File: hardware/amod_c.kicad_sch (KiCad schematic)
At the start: 209 parts, among them J1001 SMA, J1002 SMA, J1003 CE, J101 USB-C, J102 rails, J1101 SMA, J1102 SMA, J1201 SMA, J1202 SMA, J201 SMA, J202 SMA, J203 SMA, J204 SMA, J301 SMA, J302 SMA, J401 SMA, J402 SMA, J501 SMA, J502 SMA, J601 SMA, J602 SMA, J603 SMA, J701 SMA, J702 SMA, J801 SMA, J802 SMA, J901 SMA, J902 SMA, J903 SMA, J904 Pmod, Q1001 AO3401A, Q1002 DMMT3904W, Q1003 MMBT3904, Q1101 AO3401A, Q1201 AO3401A, Q201 AO3401A, Q202 AO3400A, Q301 AO3401A, Q401 AO3401A, Q501 AO3401A, Q601 AO3401A, Q701 AO3401A, Q801 AO3401A, Q901 AO3401A, Q902 BCM857BS, Q903 DMMT3904W, Q904 MMBT3904, SW1001 ON, SW1101 ON, SW1201 ON, SW201 ON, SW301 ON, SW401 ON, SW501 ON, SW601 ON, SW701 ON, SW801 ON, SW901 ON, U101 LM2664, U102 3.3V, U1101 TLC555, U1201 OPA2197, U201 TLV62568, U202 TPS7A2033, U203 OPA810, U301 LV1T34, U302 ICL7660A, U401 MAX7410, U402 LV1T34, U501 TMUX4053, U502 OPA810, U601 OPA2810, U602 TLV3501, U603 74LVC1G79, U604 74LVC1G3157, U605 74LVC1G3157, U701 LF398, U801 TLV3201, U901 OPA810

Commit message: AMOD-C: DRC 0 (Prompt 19). The Pmod's eight lines in lanes that never cross (the IOs reassigned so they nest: c5 IO8/IO4, c4 IO3, c8 IO2 down the left margin; c6 IO1/IO7, c7 IO5, c3 IO6 along the bottom); c6's bit and clock routed to its corner; the scope ground loops in the right margin
Co-Authored-By: Claude Opus 5.5 <noreply@anthropic.com>
Claude-Session: https://claude.ai/code/session_01RKeoKvFFzjk3cEBLCXXHnB
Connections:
- net PMOD1: now also U603.2 (C); no longer U701.11 (Hold)
- net PMOD5: now also U701.11 (Hold); no longer U603.2 (C)
- net PMOD6: now also U301.2 (A); no longer U603.4 (Q), U604.6 (S), U605.6 (S)
- net PMOD7: now also U603.4 (Q), U604.6 (S), U605.6 (S); no longer U301.2 (A)
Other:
- note added: "Clock IO1 at about 1 MHz and count IO7's ones. The second integrator pushes the quantization noise up at 40 dB per"
- note added: "EXPECT: OUT follows IN while IO5 is high and holds when it falls: 4 us to acquire, about 30 mV/s of droop, a few mV of hold step"
- note added: "EXPECT: a one-bit stream on IO7 whose density follows IN (+-1.65 V full scale), its noise shaped at 40 dB per decade"
- note added: "EXPECT: about -5 V on the output, falling with load as 1 / (f C) + the switches: 2 k at 1 kHz, 80 ohm at 100 kHz (the pump at half IO6's clock)"
- note added: "ICL7660A: switches charge the flying 1 uF across the supply and dump it, upside down, into the output's 1 uF. IO6"
- note added: "holding, and the aperture delay against the FPGA's edge on IO5."
- note removed: "Clock IO5 at about 1 MHz and count IO6's ones. The second integrator pushes the quantization noise up at 40 dB per"
- note removed: "EXPECT: OUT follows IN while IO1 is high and holds when it falls: 4 us to acquire, about 30 mV/s of droop, a few mV of hold step"
- note removed: "EXPECT: a one-bit stream on IO6 whose density follows IN (+-1.5 V full scale), its noise shaped at 40 dB per decade"
- note removed: "EXPECT: about -5 V on the output, falling with load as 1 / (f C) + the switches: 2 k at 1 kHz, 80 ohm at 100 kHz (the pump at half IO7's clock)"
- note removed: "ICL7660A: switches charge the flying 1 uF across the supply and dump it, upside down, into the output's 1 uF. IO7"
- note removed: "holding, and the aperture delay against the FPGA's edge on IO1."
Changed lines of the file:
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@@
 		)
 	)
-	(text "ICL7660A: switches charge the flying 1 uF across the supply and dump it, upside down, into the output's 1 uF.  IO7"
+	(text "ICL7660A: switches charge the flying 1 uF across the supply and dump it, upside down, into the output's 1 uF.  IO6"
 		(exclude_from_sim no)
 		(at 599.44 401.22 0)
@@
 		)
 	)
-	(text "holding, and the aperture delay against the FPGA's edge on IO1."
+	(text "holding, and the aperture delay against the FPGA's edge on IO5."
 		(exclude_from_sim no)
 		(at 599.44 530.86 0)
@@
 		)
 	)
-	(text "EXPECT: a one-bit stream on IO6 whose density follows IN (+-1.5 V full scale), its noise shaped at 40 dB per decade"
+	(text "EXPECT: a one-bit stream on IO7 whose density follows IN (+-1.65 V full scale), its noise shaped at 40 dB per decade"
 		(exclude_from_sim no)
 		(at 218.44 271.58 0)
@@
 		)
 	)
-	(text "EXPECT: about -5 V on the output, falling with load as 1 / (f C) + the switches: 2 k at 1 kHz, 80 ohm at 100 kHz (the pump at half IO7's clock)"
+	(text "Clock IO1 at about 1 MHz and count IO7's ones.  The second integrator pushes the quantization noise up at 40 dB per"
+		(exclude_from_sim no)
+		(at 218.44 274.22 0)
+		(effects
+			(font
+				(size 1.2 1.2)
+			)
+			(justify left)
+		)
+	)
+	(text "EXPECT: about -5 V on the output, falling with load as 1 / (f C) + the switches: 2 k at 1 kHz, 80 ohm at 100 kHz (the pump at half IO6's clock)"
 		(exclude_from_sim no)
 		(at 599.44 398.58 0)
@@
 		)
 	)
-	(text "Clock IO5 at about 1 MHz and count IO6's ones.  The second integrator pushes the quantization noise up at 40 dB per"
-		(exclude_from_sim no)
-		(at 218.44 274.22 0)
-		(effects
-			(font
-				(size 1.2 1.2)
-			)
-			(justify left)
-		)
-	)
 	(text "tutorial Trading speed for bits   (+-5 V)"
 		(exclude_from_sim no)
@@
 		)
 	)
-	(text "EXPECT: OUT follows IN while IO1 is high and holds when it falls: 4 us to acquire, about 30 mV/s of droop, a few mV of hold step"
+	(text "EXPECT: OUT follows IN while IO5 is high and holds when it falls: 4 us to acquire, about 30 mV/s of droop, a few mV of hold step"
 		(exclude_from_sim no)
 		(at 599.44 522.94 0)
@@
 		)
 	)
-	(label "PMOD6"
-		(at 449.58 198.12 0)
-		(effects
-			(font
-				(size 1.27 1.27)
-			)
-			(justify left)
-		)
-	)
 	(label "c5_VS"
 		(at 289.56 101.6 180)
@@
 		)
 	)
-	(label "PMOD6"
-		(at 500.38 200.66 180)
-		(effects
-			(font
-				(size 1.27 1.27)
-			)
-			(justify right)
-		)
-	)
 	(label "c9_MO"
 		(at 129.54 461.01 0)
@@
 		)
 	)
+	(label "PMOD7"
+		(at 449.58 198.12 0)
+		(effects
+			(font
+				(size 1.27 1.27)
+			)
+			(justify left)
+		)
+	)
 	(label "c5_OA"
 		(at 363.22 101.6 0)
@@
 		)
 	)
+	(label "PMOD1"
+		(at 419.1 208.28 180)
+		(effects
+			(font
+				(size 1.27 1.27)
+			)
+			(justify right)
+		)
+	)
 	(label "c7_VS"
 		(at 688.34 447.04 0)
@@
 		)
 	)
+	(label "PMOD7"
+		(at 464.82 200.66 180)
+		(effects
+			(font
+				(size 1.27 1.27)
+			)
+			(justify right)
+		)
+	)
 	(label "c5_VS"
 		(at 360.68 73.66 0)
@@
 		)
 	)
-	(label "PMOD1"
-		(at 680.72 457.2 180)
-		(effects
-			(font
-				(size 1.27 1.27)
-			)
-			(justify right)
-		)
-	)
 	(label "c1_CC1"
 		(at 660.4 180.34 0)
@@
 		)
 	)
+	(label "PMOD5"
+		(at 680.72 457.2 180)
+		(effects
+			(font
+				(size 1.27 1.27)
+			)
+			(justify right)
+		)
+	)
 	(label "c2_VS"
 		(at 287.02 322.58 0)
@@
 		)
 	)
-	(label "PMOD5"
-		(at 419.1 208.28 180)
-		(effects
-			(font
-				(size 1.27 1.27)
-			)
-			(justify right)
-		)
-	)
 	(label "c1_LEDR"
 		(at 642.62 254 180)
@@
 		)
 	)
-	(label "PMOD6"
-		(at 464.82 200.66 180)
-		(effects
-			(font
-				(size 1.27 1.27)
-			)
-			(justify right)
-		)
-	)
 	(label "c5_G"
 		(at 248.92 76.2 180)
@@
 		)
 	)
+	(label "PMOD6"
+		(at 680.72 330.2 180)
+		(effects
+			(font
+				(size 1.27 1.27)
+			)
+			(justify right)
+		)
+	)
 	(label "c8_VS"
 		(at 129.54 327.66 0)
@@
 		)
 	)
-	(label "PMOD7"
-		(at 680.72 330.2 180)
+	(label "c2_GATE"
+		(at 373.38 365.76 0)
 		(effects
 			(font
 				(size 1.27 1.27)
 			)
-			(justify right)
+			(justify left)
 		)
 	)
-	(label "c2_GATE"
-		(at 373.38 365.76 0)
+	(label "PMOD7"
+		(at 500.38 200.66 180)
 		(effects
 			(font
 				(size 1.27 1.27)
 			)
-			(justify left)
+			(justify right)
 		)
 	)

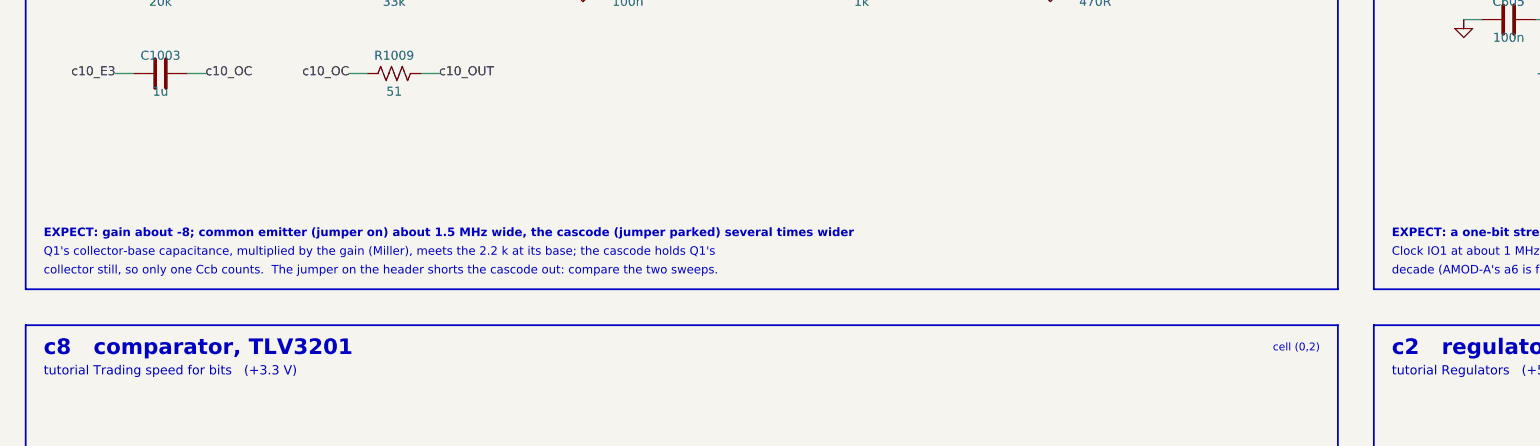
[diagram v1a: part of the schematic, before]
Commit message: AMOD-C: handbook, tile docs, Pmod line names and the README's table; JLCPCB rotations for its fifteen new codes (check_rotations: 209 codes, 0 differ); c10's gain stated from IN (-6) as well as at the collector; fab package
Co-Authored-By: Claude Opus 5.5 <noreply@anthropic.com>
Claude-Session: https://claude.ai/code/session_01RKeoKvFFzjk3cEBLCXXHnB
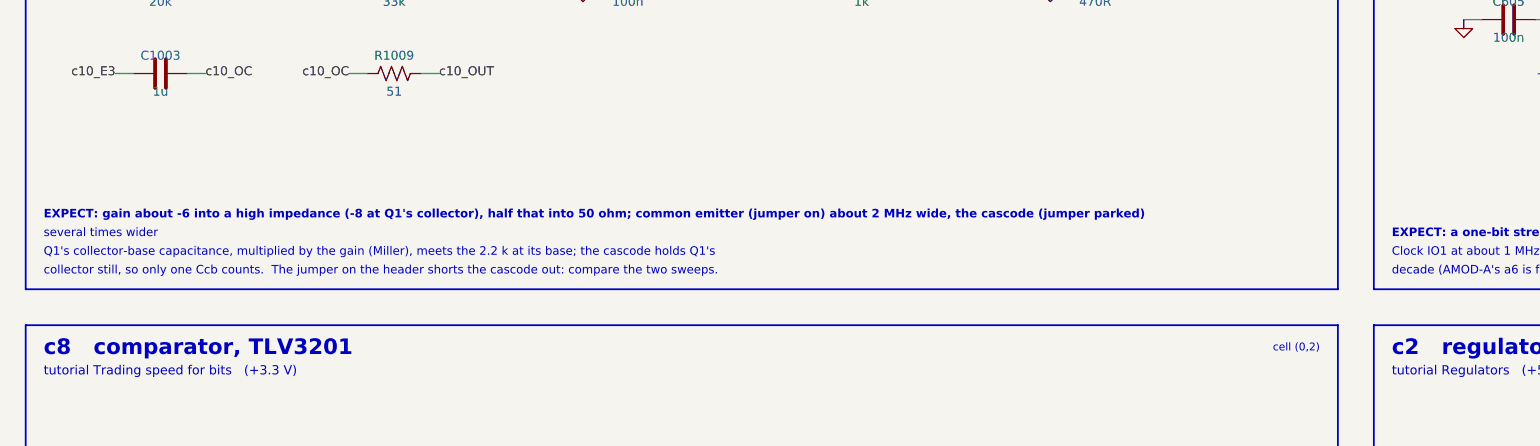
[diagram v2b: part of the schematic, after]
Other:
- note added: "EXPECT: gain about -6 into a high impedance (-8 at Q1's collector), half that into 50 ohm; common emitter (jumper on) about 2 MHz wide, the cascode (jumper parked)"
- note added: "several times wider"
- note removed: "EXPECT: gain about -8; common emitter (jumper on) about 1.5 MHz wide, the cascode (jumper parked) several times wider"
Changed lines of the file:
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@@
+		)
+	)
+	(text "Q1's collector-base capacitance, multiplied by the gain (Miller), meets the 2.2 k at its base; the cascode holds Q1's"
+		(exclude_from_sim no)
+		(at 27.94 274.22 0)
+		(effects
+			(font
+				(size 1.2 1.2)
+			)
+			(justify left)
 		)
 	)
@@
 		)
 	)
+	(text "several times wider"
+		(exclude_from_sim no)
+		(at 27.94 271.58 0)
+		(effects
+			(font
+				(size 1.2 1.2)
+			)
+			(justify left)
+		)
+	)
 	(text "±1 V"
 		(exclude_from_sim no)
@@
 		)
 	)
-	(text "Q1's collector-base capacitance, multiplied by the gain (Miller), meets the 2.2 k at its base; the cascode holds Q1's"
-		(exclude_from_sim no)
-		(at 27.94 274.22 0)
-		(effects
-			(font
-				(size 1.2 1.2)
-			)
-			(justify left)
-		)
-	)
 	(text "INT1"
 		(exclude_from_sim no)
@@
 		)
 	)
-	(text "EXPECT: gain about -8; common emitter (jumper on) about 1.5 MHz wide, the cascode (jumper parked) several times wider"
-		(exclude_from_sim no)
-		(at 27.94 271.58 0)
-		(effects
-			(font
-				(size 1.2 1.2)
-				(bold yes)
-			)
-			(justify left)
-		)
-	)
 	(text "slope gm = Itail / (4 VT), about 10 mS here; a triangle in becomes a sine-like wave out when it is driven past balance."
 		(exclude_from_sim no)
@@
 		)
 	)
+	(text "EXPECT: gain about -6 into a high impedance (-8 at Q1's collector), half that into 50 ohm; common emitter (jumper on) about 2 MHz wide, the cascode (jumper parked)"
+		(exclude_from_sim no)
+		(at 27.94 268.94 0)
+		(effects
+			(font
+				(size 1.2 1.2)
+				(bold yes)
+			)
+			(justify left)
+		)
+	)

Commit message: Two pinouts read against their datasheets and fixed: the DMMT3904W (AMOD-C's c9 and c10) is 1 B2, 2 B1, 3 C1, 4 E1, 5 E2, 6 C2, not the BCM857BS's order (c9's pair turned 180 with IN+ under it on the back, c10's turned 180 with Q1's base on the back); RF-MOD's 915 MHz SAW has its output on pad 4, not 3 (r4 took it from a ground pad). scripts/check_pinouts.py compares every symbol's pin names with EasyEDA's: these two were its only real disagreements
Co-Authored-By: Claude Opus 5.5 <noreply@anthropic.com>
Claude-Session: https://claude.ai/code/session_01RKeoKvFFzjk3cEBLCXXHnB
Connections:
- net c10_C1: now also Q1002.3 (C1), Q1002.5 (E2); no longer Q1002.4 (E2), Q1002.6 (C1)
- net c10_CB: now also Q1002.1 (B2); no longer Q1002.5 (B2)
- net c10_CN: now also Q1002.6 (C2); no longer Q1002.3 (C2)
- net c10_E1: now also Q1002.4 (E1); no longer Q1002.1 (E1)
- net c9_EM: now also Q903.5 (E2); no longer Q903.1 (E1)
- net c9_INN: now also Q903.1 (B2); no longer Q903.5 (B2)
- net c9_MD: now also Q903.3 (C1); no longer Q903.6 (C1)
- net c9_MO: now also Q903.6 (C2); no longer Q903.3 (C2)
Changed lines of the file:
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@@
 		(pin "2"
 		)
-		(pin "5"
-		)
-		(pin "6"
-		)
 		(pin "1"
 		)
@@
 		(pin "4"
 		)
+		(pin "6"
+		)
+		(pin "5"
+		)
 		(instances
 			(project "amod_c"
@@
 		(pin "2"
 		)
-		(pin "5"
-		)
-		(pin "6"
-		)
 		(pin "1"
 		)
@@
 		(pin "4"
 		)
+		(pin "6"
+		)
+		(pin "5"
+		)
 		(instances

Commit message: AMOD-C: c6's second integrator 680 pF (half the swing, the same bits: the comparator sees only its sign) and 10 k into the comparator's +IN, so the 3.3 V comparator survives an integrator at a rail; c2's LOAD reaches its op amp (whose negative rail is ground) through 1 k. Simulated: c6's second output stays inside 0-3.3 V up to 1.5 V in
Co-Authored-By: Claude Opus 5.5 <noreply@anthropic.com>
Claude-Session: https://claude.ai/code/session_01RKeoKvFFzjk3cEBLCXXHnB
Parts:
- added R210: 10R, Resistor_SMD:R_0805_2012Metric, symbol Device:R_US
- added R612: 1k, Resistor_SMD:R_0402_1005Metric, symbol Device:R_US
- C603: value 330p -> 680p; LCSC C190579 -> C301953; MPN 0402CG331J500NT -> 0402CG681J500NT
- R208: value 100R -> 1k; LCSC C25076 -> C11702; MPN 0402WGF1000TCE -> 0402WGF1001TCE
- R209: value 10R -> 100R; footprint Resistor_SMD:R_0805_2012Metric -> Resistor_SMD:R_0402_1005Metric; LCSC C17415 -> C25076; MPN 0805W8F100JT5E -> 0402WGF1000TCE
- R608: footprint Resistor_SMD:R_0603_1608Metric -> Resistor_SMD:R_0402_1005Metric; LCSC C95204 -> C25744; MPN RT0603BRD0710KL -> 0402WGF1002TCE
- R610: value 3.3k -> 10k; footprint Resistor_SMD:R_0402_1005Metric -> Resistor_SMD:R_0603_1608Metric; LCSC C25890 -> C95204; MPN 0402WGF3301TCE -> RT0603BRD0710KL
- R611: value 1k -> 3.3k; LCSC C11702 -> C25890; MPN 0402WGF1001TCE -> 0402WGF3301TCE
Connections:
- net +3V3: now also R609.1; no longer R608.1
- net GND: now also R610.2, R210.1, R612.1; no longer R209.1, R609.2, R611.1
- net c2_FBK: now also R208.2; no longer R207.2
- net c2_GATE: now also R209.2; no longer R208.2
- net c2_LOAD: now also R207.1; no longer U203.3 (+IN)
- net c2_OG: now also R209.1; no longer R208.1
- net c2_SH: now also R208.1, R210.2; no longer R207.1, R209.2
- net c6_I2: now also R608.1, R611.1; no longer R610.1, U602.3 (+)
- net c6_I2J: now also R612.2; no longer R610.2
- net c6_VM: now also R609.2, R610.1; no longer R608.2, R609.1
- new net c2_LIN: R207.2, U203.3 (+IN)
- new net c6_I2C: R608.2, U602.3 (+)
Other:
- moved on the sheet: C207, C208, C606, C607, C608, R207, R608, R610, U602, U603, U604, U605

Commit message: Pre-order checks from CLAUDE_PCB.md's new lessons (Prompt 21): the KF301 terminals turned for their wire openings (CPL +180, body 3.7 / 4.0, a wire-face check), four oversold parts swapped (27R, 6.8k, 220n, OPA847IDBVT at its own +180), fourteen vias moved out of SMD pads (check_layout.py gates it and RF detours), 200-250 mW terminations, assembly drawings from Fab and silk fitted to Letter (fit_pdf.py from CostasLink), the stock gate on JLCPCB's free count, electrolytics in the rotation check, the RF gates surveyed (rf_extract.py, rf_survey.py) and written into the DOA lists; all nine boards rebuilt: ERC 0, DRC 0, every check
Co-Authored-By: Claude Opus 5.5 <noreply@anthropic.com>
Claude-Session: https://claude.ai/code/session_01RKeoKvFFzjk3cEBLCXXHnB
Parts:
- R1207, R205, R206, R401, R404, R501, R701, R702, R901, R902, R907: LCSC C25120 -> C844112; MPN 0402WGF499JTCE -> CRCW040249R9FKEDHP
- R204, R503: LCSC C23185 -> C6230117; MPN 0603WAF499JT5E -> SR0603FR-7T49R9L
- R604, R903: LCSC C25917 -> C93940; MPN 0402WGF6801TCE -> RC0402FR-076K8L
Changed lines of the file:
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@@
 			)
 		)
-		(property "LCSC" "C25120"
+		(property "LCSC" "C844112"
 			(at 234.95 365.76 90)
 			(hide yes)
@@
 			)
 		)
-		(property "MPN" "0402WGF499JTCE"
+		(property "MPN" "CRCW040249R9FKEDHP"
 			(at 234.95 365.76 90)
 			(hide yes)
@@
 			)
 		)
-		(property "LCSC" "C25917"
+		(property "LCSC" "C93940"
 			(at 105.41 480.06 90)
 			(hide yes)
@@
 			)
 		)
-		(property "MPN" "0402WGF6801TCE"
+		(property "MPN" "RC0402FR-076K8L"
 			(at 105.41 480.06 90)
 			(hide yes)
@@
 			)
 		)
-		(property "LCSC" "C25120"
+		(property "LCSC" "C844112"
 			(at 44.45 101.6 90)
 			(hide yes)
@@
 			)
 		)
-		(property "MPN" "0402WGF499JTCE"
+		(property "MPN" "CRCW040249R9FKEDHP"
 			(at 44.45 101.6 90)
 			(hide yes)
@@
 			)
 		)
-		(property "LCSC" "C25120"
+		(property "LCSC" "C844112"
 			(at 615.95 480.06 90)
 			(hide yes)
@@
 			)
 		)
-		(property "MPN" "0402WGF499JTCE"
+		(property "MPN" "CRCW040249R9FKEDHP"
 			(at 615.95 480.06 90)
 			(hide yes)
@@
 			)
 		)
-		(property "LCSC" "C25120"
+		(property "LCSC" "C844112"
 			(at 288.29 480.06 90)
 			(hide yes)
@@
 			)
 		)
-		(property "MPN" "0402WGF499JTCE"
+		(property "MPN" "CRCW040249R9FKEDHP"
 			(at 288.29 480.06 90)
 			(hide yes)
@@
 			)
 		)
-		(property "LCSC" "C25120"
+		(property "LCSC" "C844112"
 			(at 110.49 114.3 90)
 			(hide yes)
@@
 			)
 		)
-		(property "MPN" "0402WGF499JTCE"
+		(property "MPN" "CRCW040249R9FKEDHP"
 			(at 110.49 114.3 90)
 			(hide yes)
@@
 			)
 		)
-		(property "LCSC" "C23185"
+		(property "LCSC" "C6230117"
 			(at 466.09 353.06 90)
 			(hide yes)
@@
 			)
 		)
-		(property "MPN" "0603WAF499JT5E"
+		(property "MPN" "SR0603FR-7T49R9L"
 			(at 466.09 353.06 90)
 			(hide yes)
@@
 			)
 		)
-		(property "LCSC" "C25917"
+		(property "LCSC" "C93940"
 			(at 417.83 228.6 90)
 			(hide yes)
@@
 			)
 		)
-		(property "MPN" "0402WGF6801TCE"
+		(property "MPN" "RC0402FR-076K8L"
 			(at 417.83 228.6 90)
 			(hide yes)
@@
 			)
 		)
-		(property "LCSC" "C25120"
+		(property "LCSC" "C844112"
 			(at 676.91 480.06 90)
 			(hide yes)
@@
 			)
 		)
-		(property "MPN" "0402WGF499JTCE"
+		(property "MPN" "CRCW040249R9FKEDHP"
 			(at 676.91 480.06 90)
 			(hide yes)
@@
 			)
 		)
-		(property "LCSC" "C25120"
+		(property "LCSC" "C844112"
 			(at 458.47 520.7 90)
 			(hide yes)
@@
 			)
 		)
-		(property "MPN" "0402WGF499JTCE"
+		(property "MPN" "CRCW040249R9FKEDHP"
 			(at 458.47 520.7 90)
 			(hide yes)
@@
 			)
 		)
-		(property "LCSC" "C25120"
+		(property "LCSC" "C844112"
 			(at 74.93 480.06 90)
 			(hide yes)
@@
 			)
 		)
-		(property "MPN" "0402WGF499JTCE"
+		(property "MPN" "CRCW040249R9FKEDHP"
 			(at 74.93 480.06 90)
 			(hide yes)
@@
 			)
 		)
-		(property "LCSC" "C25120"
+		(property "LCSC" "C844112"
 			(at 234.95 101.6 90)
 			(hide yes)
@@
 			)
 		)
-		(property "MPN" "0402WGF499JTCE"
+		(property "MPN" "CRCW040249R9FKEDHP"
 			(at 234.95 101.6 90)
 			(hide yes)
@@
 			)
 		)
-		(property "LCSC" "C23185"
+		(property "LCSC" "C6230117"
 			(at 417.83 101.6 90)
 			(hide yes)
@@
 			)
 		)
-		(property "MPN" "0603WAF499JT5E"
+		(property "MPN" "SR0603FR-7T49R9L"
 			(at 417.83 101.6 90)
 			(hide yes)
@@
 			)
 		)
-		(property "LCSC" "C25120"
+		(property "LCSC" "C844112"
 			(at 267.97 365.76 90)
 			(hide yes)
@@
 			)
 		)
-		(property "MPN" "0402WGF499JTCE"
+		(property "MPN" "CRCW040249R9FKEDHP"
 			(at 267.97 365.76 90)
 			(hide yes)
@@
 			)
 		)
-		(property "LCSC" "C25120"
+		(property "LCSC" "C844112"
 			(at 44.45 480.06 90)
 			(hide yes)
@@
 			)
 		)
-		(property "MPN" "0402WGF499JTCE"
+		(property "MPN" "CRCW040249R9FKEDHP"
 			(at 44.45 480.06 90)
 			(hide yes)
